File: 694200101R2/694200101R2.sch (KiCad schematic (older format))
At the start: 264 parts, among them J1 USB_C_Receptacle_USB2.0, J2 Conn_01x06_Male, SW1 MX_SW, SW10 MX_SW, SW100 MX_SW, SW101 MX_SW, SW102 MX_SW, SW103 MX_SW, SW104 MX_SW, SW105 MX_SW, SW106 MX_SW, SW107 MX_SW, SW108 SW_SPST, SW109 SW_SPDT, SW11 MX_SW, SW12 MX_SW, SW13 MX_SW, SW14 MX_SW, SW15 MX_SW, SW16 MX_SW, SW17 MX_SW, SW18 MX_SW, SW19 MX_SW, SW2 MX_SW, SW20 MX_SW, SW21 MX_SW, SW22 MX_SW, SW23 MX_SW, SW24 MX_SW, SW25 MX_SW, SW26 MX_SW, SW27 MX_SW, SW28 MX_SW, SW29 MX_SW, SW3 MX_SW, SW30 MX_SW, SW31 MX_SW, SW32 MX_SW, SW33 MX_SW, SW34 MX_SW, SW35 MX_SW, SW36 MX_SW, SW37 MX_SW, SW38 MX_SW, SW39 MX_SW, SW4 MX_SW, SW40 MX_SW, SW41 MX_SW, SW42 MX_SW, SW43 MX_SW, SW44 MX_SW, SW45 MX_SW, SW46 MX_SW, SW47 MX_SW, SW48 MX_SW, SW49 MX_SW, SW5 MX_SW, SW50 MX_SW, SW51 MX_SW, SW52 MX_SW, SW53 MX_SW, SW54 MX_SW, SW55 MX_SW, SW56 MX_SW, SW57 MX_SW, SW58 MX_SW, SW59 MX_SW, SW6 MX_SW, SW60 MX_SW, SW61 MX_SW, SW62 MX_SW, SW63 MX_SW, SW64 MX_SW, SW65 MX_SW, SW66 MX_SW, SW67 MX_SW, SW68 MX_SW, SW69 MX_SW, SW7 MX_SW, SW70 MX_SW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

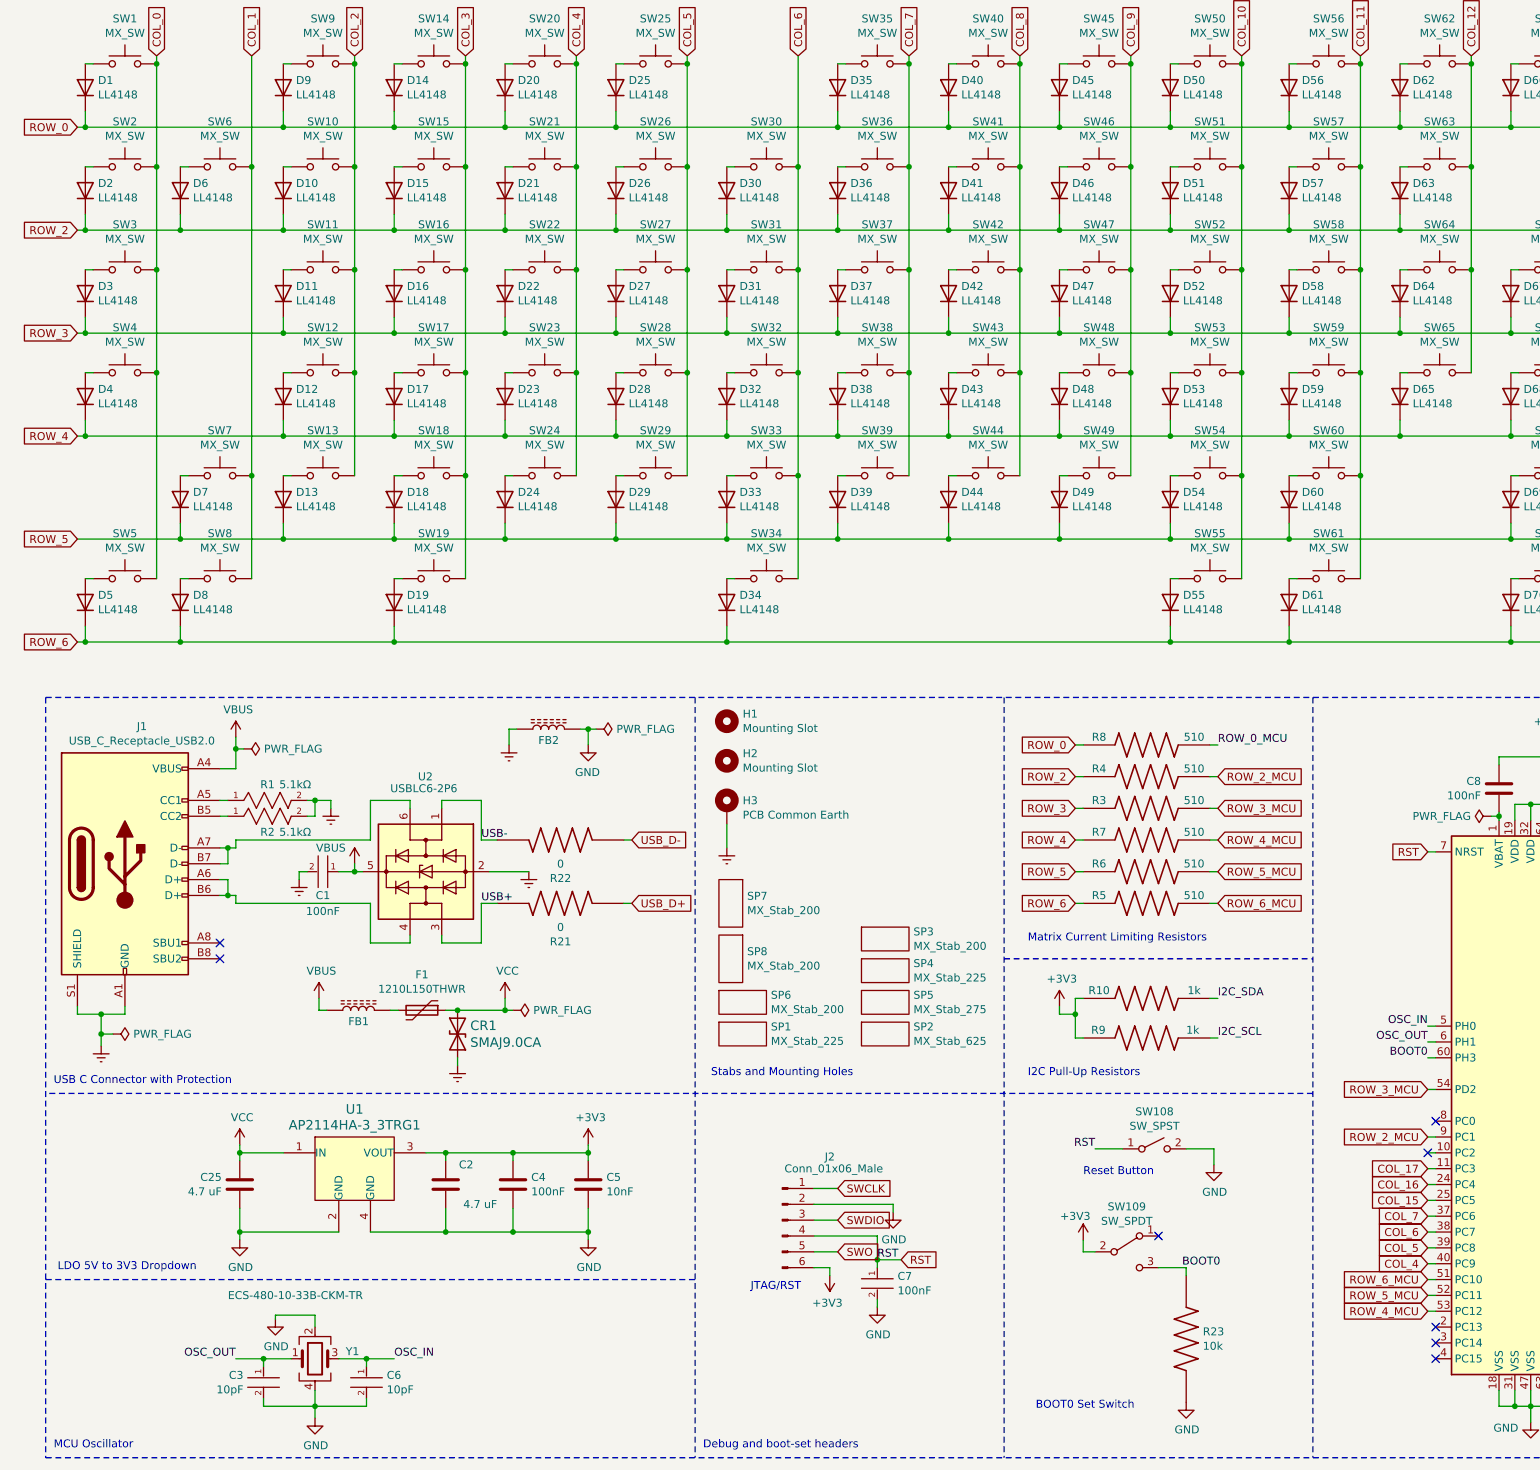
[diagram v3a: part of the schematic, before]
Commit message: Rename row labels
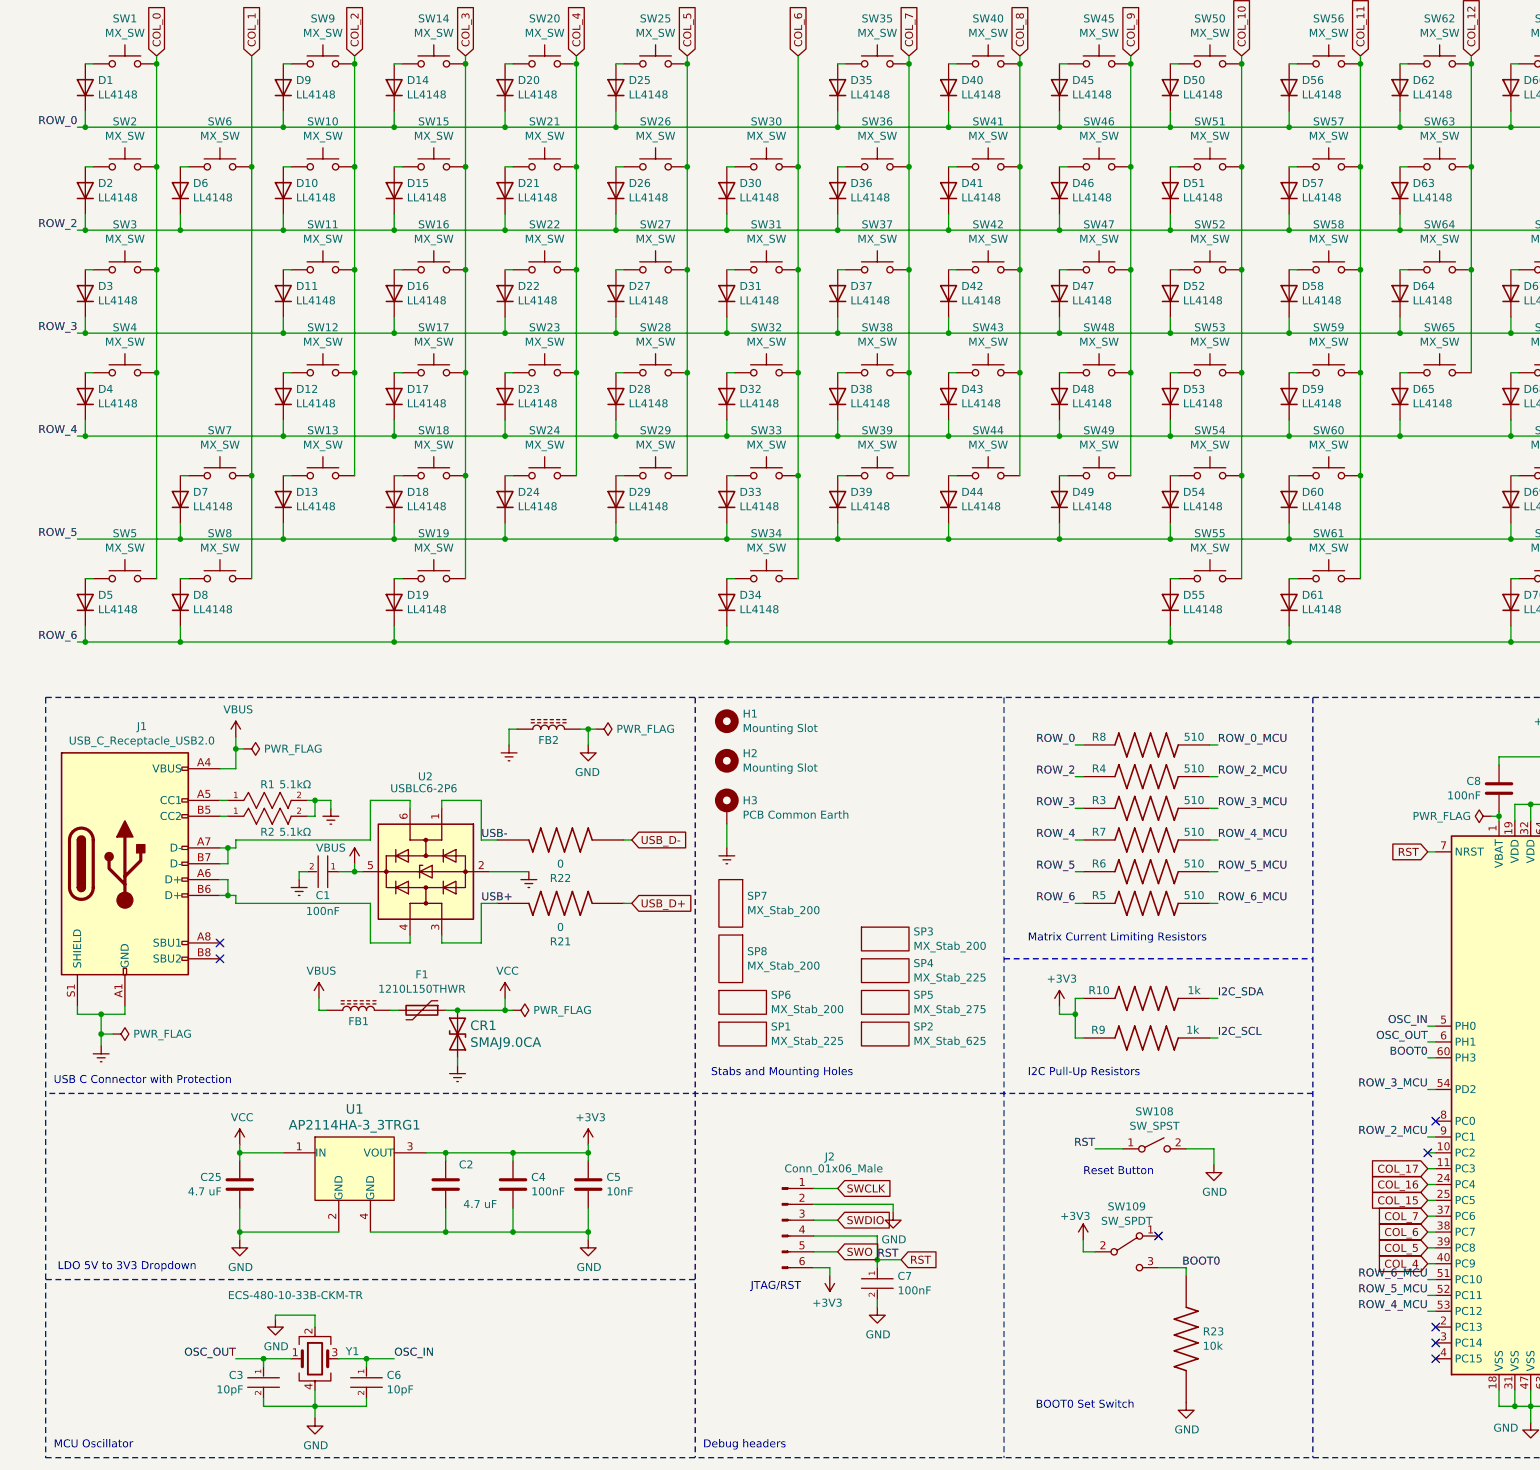
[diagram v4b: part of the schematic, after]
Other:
- note added: "Debug headers"
- note removed: "Debug and boot-set headers"
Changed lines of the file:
@@
 	1    0    0    -1
 $EndComp
-Text GLabel 850  1300 0    50   Input ~ 0
-ROW_0
 Text GLabel 1350 850  1    50   Input ~ 0
 COL_0
@@
 Wire Wire Line
 	900  3150 900  3250
-Text GLabel 850  1950 0    50   Input ~ 0
-ROW_2
-Text GLabel 850  2600 0    50   Input ~ 0
-ROW_3
-Text GLabel 850  3250 0    50   Input ~ 0
-ROW_4
-Text GLabel 850  3900 0    50   Input ~ 0
-ROW_5
-Text GLabel 850  4550 0    50   Input ~ 0
-ROW_6
 Text GLabel 1950 850  1    50   Input ~ 0
 COL_1
@@
 Text GLabel 10775 7375 2    50   Input ~ 0
 COL_0
-Text GLabel 7150 6200 0    50   Input ~ 0
-ROW_6
-Text GLabel 7150 6000 0    50   Input ~ 0
-ROW_5
-Text GLabel 7150 5800 0    50   Input ~ 0
-ROW_4
-Text GLabel 7150 5600 0    50   Input ~ 0
-ROW_3
-Text GLabel 7150 5200 0    50   Input ~ 0
-ROW_0
 $Comp
 L power:+3V3 #PWR014
@@
 Wire Wire Line
 	9825 5275 10125 5275
-Text GLabel 8050 5600 2    50   Input ~ 0
-ROW_3_MCU
 Wire Wire Line
 	8000 5600 8050 5600
-Text GLabel 9375 7375 0    50   Input ~ 0
-ROW_3_MCU
-Text GLabel 9375 7675 0    50   Input ~ 0
-ROW_2_MCU
-Text GLabel 9375 8575 0    50   Input ~ 0
-ROW_6_MCU
-Text GLabel 8050 6200 2    50   Input ~ 0
-ROW_6_MCU
 Wire Wire Line
 	8000 6200 8050 6200
-Text GLabel 8050 6000 2    50   Input ~ 0
-ROW_5_MCU
-Text GLabel 9375 8675 0    50   Input ~ 0
-ROW_5_MCU
-Text GLabel 8050 5800 2    50   Input ~ 0
-ROW_4_MCU
-Text GLabel 9375 8775 0    50   Input ~ 0
-ROW_4_MCU
 Wire Wire Line
 	8000 5400 8050 5400
-Text GLabel 8050 5400 2    50   Input ~ 0
-ROW_2_MCU
 $Comp
 L Resistor-Lib:RMCF0805FT510R R4
@@
 	1    0    0    -1
 $EndComp
-Text GLabel 7150 5400 0    50   Input ~ 0
-ROW_2
 Wire Wire Line
 	7200 5400 7150 5400
@@
 Encoder
 Text Notes 4800 9650 0    50   ~ 0
-Debug and boot-set headers
+Debug headers
 $Comp
 L power:PWR_FLAG #FLG0101
@@
 	9775 5650 9825 5650
 Connection ~ 9825 5650
-NoConn ~ 9375 7775
 NoConn ~ 10775 7975
 $Comp
@@
 Wire Wire Line
 	2025 9075 2200 9075
+Text Label 8050 5400 0    50   ~ 0
+ROW_2_MCU
+Text Label 8050 5600 0    50   ~ 0
+ROW_3_MCU
+Text Label 8050 5800 0    50   ~ 0
+ROW_4_MCU
+Text Label 8050 6000 0    50   ~ 0
+ROW_5_MCU
+Text Label 8050 6200 0    50   ~ 0
+ROW_6_MCU
+Text Label 9375 7675 2    50   ~ 0
+ROW_2_MCU
+Text Label 9375 7375 2    50   ~ 0
+ROW_3_MCU
+Text Label 9375 8775 2    50   ~ 0
+ROW_4_MCU
+Text Label 9375 8675 2    50   ~ 0
+ROW_5_MCU
+Text Label 9375 8575 2    50   ~ 0
+ROW_6_MCU
+Text Label 7150 5200 2    50   ~ 0
+ROW_0
+Text Label 7150 5400 2    50   ~ 0
+ROW_2
+Text Label 7150 5600 2    50   ~ 0
+ROW_3
+Text Label 7150 5800 2    50   ~ 0
+ROW_4
+Text Label 7150 6000 2    50   ~ 0
+ROW_5
+Text Label 7150 6200 2    50   ~ 0
+ROW_6
+Text Label 850  1300 2    50   ~ 0
+ROW_0
+Text Label 850  1950 2    50   ~ 0
+ROW_2
+Text Label 850  2600 2    50   ~ 0
+ROW_3
+Text Label 850  3250 2    50   ~ 0
+ROW_4
+Text Label 850  3900 2    50   ~ 0
+ROW_5
+Text Label 850  4550 2    50   ~ 0
+ROW_6
+NoConn ~ 9375 7775
 $EndSCHEMATC

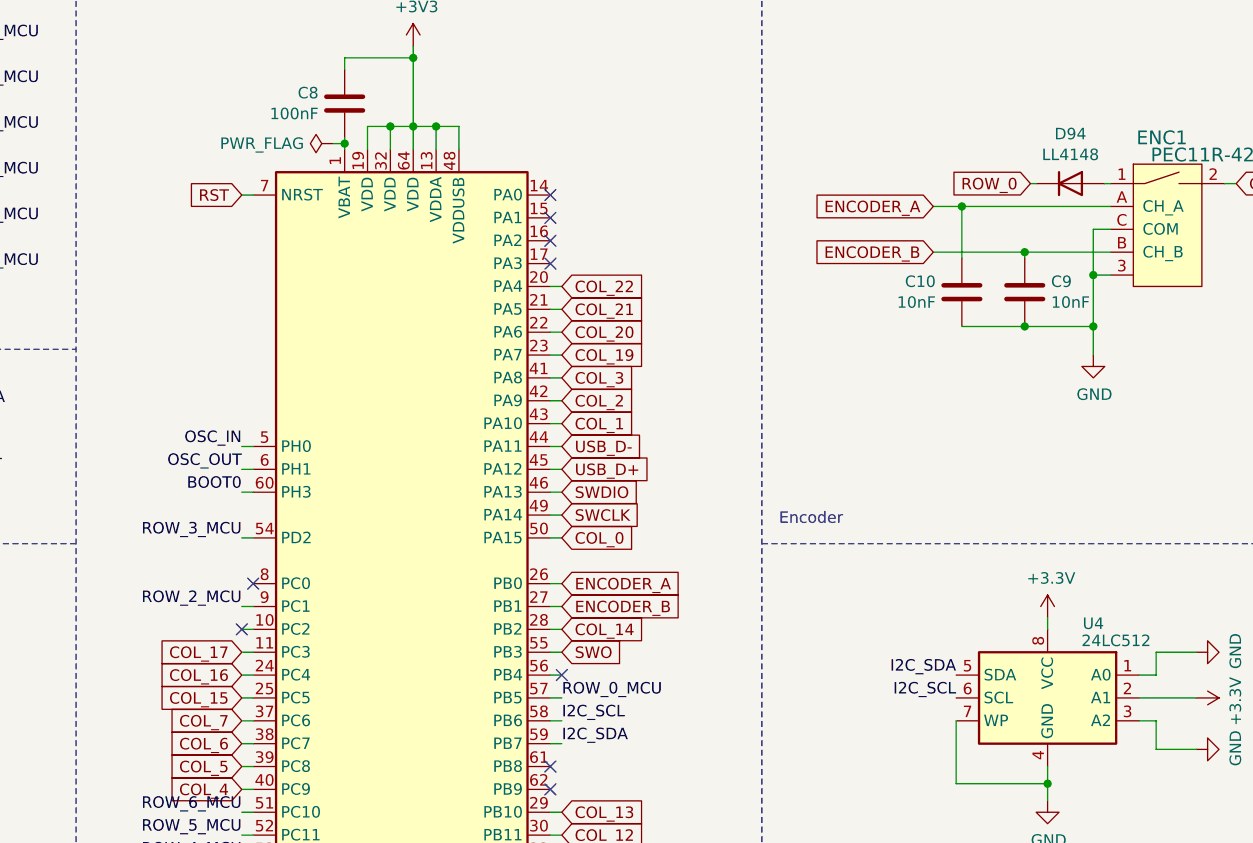
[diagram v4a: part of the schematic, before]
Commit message: Fixed Ratsnest errors from prettifying schematic
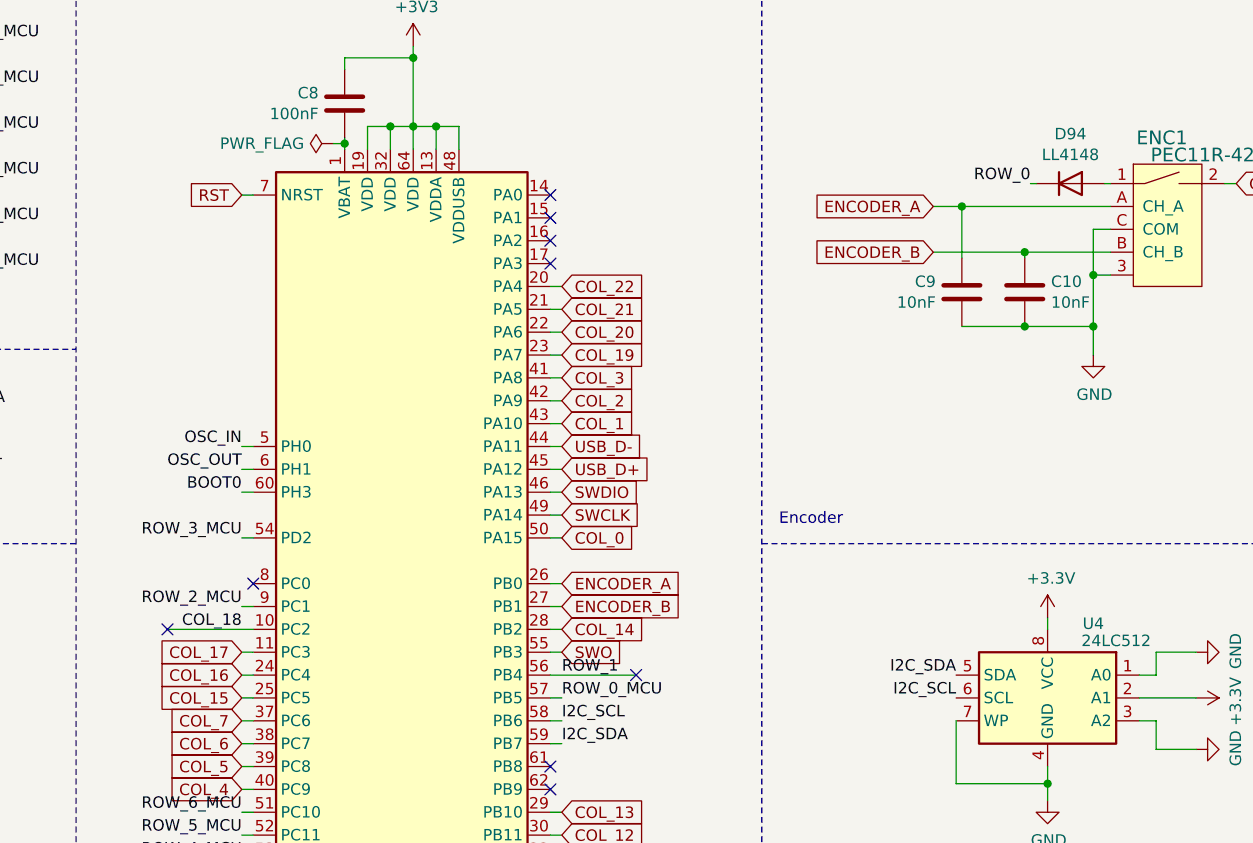
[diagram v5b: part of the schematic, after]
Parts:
- renumbered C9 to C10, C10 to C9
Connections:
- net COL_18: now reaches U3.10 (PC2)
- net ROW_1: now reaches U3.56 (PB4)
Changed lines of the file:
@@
 Wire Wire Line
 	12825 5825 12850 5825
-Text GLabel 12825 5825 0    50   Input ~ 0
-ROW_0
 Wire Wire Line
 	13175 6025 13100 6025
@@
 	12800 6125 12800 6150
 $Comp
-L Device:C C9
+L Device:C C10
 U 1 1 65C47B00
 P 12800 6300
-F 0 "C9" H 12915 6346 50  0000 L CNN
+F 0 "C10" H 12915 6346 50  0000 L CNN
 F 1 "10nF" H 12915 6255 50  0000 L CNN
 F 2 "Capacitor_SMD:C_0603_1608Metric" H 12838 6150 50  0001 C CNN
@@
 	13100 6025 13100 6225
 $Comp
-L Device:C C10
+L Device:C C9
 U 1 1 658CEFEB
 P 12525 6300
-F 0 "C10" H 12411 6346 50  0000 R CNN
+F 0 "C9" H 12411 6346 50  0000 R CNN
 F 1 "10nF" H 12411 6255 50  0000 R CNN
 F 2 "Capacitor_SMD:C_0603_1608Metric" H 12563 6150 50  0001 C CNN
@@
 	9775 5650 9825 5650
 Connection ~ 9825 5650
-NoConn ~ 10775 7975
+NoConn ~ 11100 7975
 $Comp
 L Power_Protection:USBLC6-2P6 U2
@@
 	9425 7875 9375 7875
 Wire Wire Line
-	9425 7775 9375 7775
+	9425 7775 9050 7775
 NoConn ~ 9425 9075
 NoConn ~ 9425 8975
@@
 	10725 8075 10775 8075
 Wire Wire Line
-	10725 7975 10775 7975
+	10725 7975 11100 7975
 Wire Wire Line
 	10725 7875 10775 7875
@@
 Text Label 850  4550 2    50   ~ 0
 ROW_6
-NoConn ~ 9375 7775
+NoConn ~ 9050 7775
+Text Label 12825 5825 2    50   ~ 0
+ROW_0
+Text Label 9375 7775 2    50   ~ 0
+COL_18
+Text Label 10775 7975 0    50   ~ 0
+ROW_1
 $EndSCHEMATC

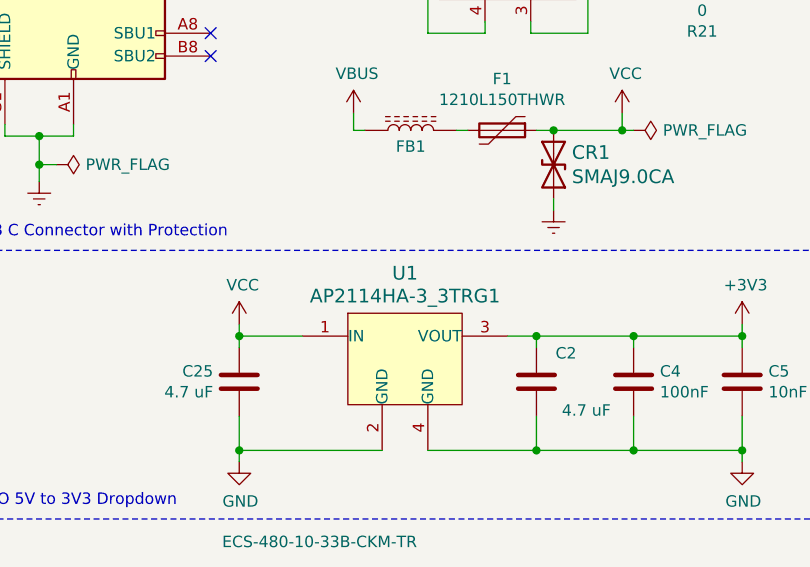
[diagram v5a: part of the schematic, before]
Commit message: Fixed Symbol for LDO
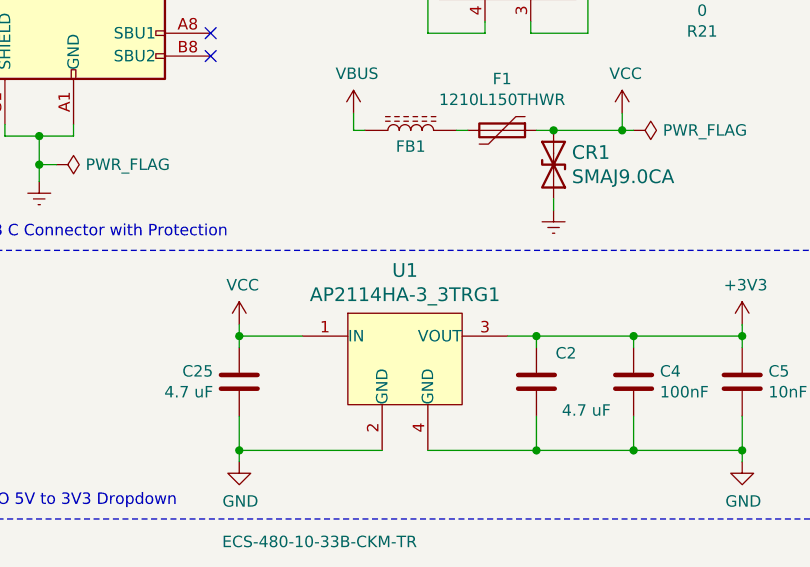
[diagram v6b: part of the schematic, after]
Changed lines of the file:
@@
-	1    0    0    -1
-$EndComp
-$Comp
-L cldg:AP2114HA-3_3TRG1 U1
-U 1 1 62A6A64D
-P 2650 7775
-F 0 "U1" H 2600 8050 60  0000 C CNN
-F 1 "AP2114HA-3_3TRG1" H 2600 7950 60  0000 C CNN
-F 2 "digikey-footprints:SOT-223" H 2850 7975 60  0001 L CNN
-F 3 "https://www.diodes.com/assets/Datasheets/AP2114.pdf" H 2850 8075 60  0001 L CNN
-F 4 "AP2114H-3.3TRG1DICT-ND" H 2850 8175 60  0001 L CNN "Digi-Key_PN"
-F 5 "AP2114H-3.3TRG1" H 2850 8275 60  0001 L CNN "MPN"
-F 6 "Integrated Circuits (ICs)" H 2850 8375 60  0001 L CNN "Category"
-F 7 "PMIC - Voltage Regulators - Linear" H 2850 8475 60  0001 L CNN "Family"
-F 8 "https://www.diodes.com/assets/Datasheets/AP2114.pdf" H 2850 8575 60  0001 L CNN "DK_Datasheet_Link"
-F 9 "/product-detail/en/diodes-incorporated/AP2114H-3.3TRG1/AP2114H-3.3TRG1DICT-ND/4505142" H 2850 8675 60  0001 L CNN "DK_Detail_Page"
-F 10 "IC REG LINEAR 3.3V 1A SOT223" H 2850 8775 60  0001 L CNN "Description"
-F 11 "Diodes Incorporated" H 2850 8875 60  0001 L CNN "Manufacturer"
-F 12 "Active" H 2850 8975 60  0001 L CNN "Status"
-	1    2650 7775
 	1    0    0    -1
 $EndComp
@@
 Text Label 10775 7975 0    50   ~ 0
 ROW_1
+$Comp
+L cldg:AP2114HA-3_3TRG1 U1
+U 1 1 632C3127
+P 2650 7775
+F 0 "U1" H 2600 8062 60  0000 C CNN
+F 1 "AP2114HA-3_3TRG1" H 2600 7956 60  0000 C CNN
+F 2 "digikey-footprints:SOT-223" H 2850 7975 60  0001 L CNN
+F 3 "https://www.diodes.com/assets/Datasheets/AP2114.pdf" H 2850 8075 60  0001 L CNN
+F 4 "AP2114H-3.3TRG1DICT-ND" H 2850 8175 60  0001 L CNN "Digi-Key_PN"
+F 5 "AP2114H-3.3TRG1" H 2850 8275 60  0001 L CNN "MPN"
+F 6 "Integrated Circuits (ICs)" H 2850 8375 60  0001 L CNN "Category"
+F 7 "PMIC - Voltage Regulators - Linear" H 2850 8475 60  0001 L CNN "Family"
+F 8 "https://www.diodes.com/assets/Datasheets/AP2114.pdf" H 2850 8575 60  0001 L CNN "DK_Datasheet_Link"
+F 9 "/product-detail/en/diodes-incorporated/AP2114H-3.3TRG1/AP2114H-3.3TRG1DICT-ND/4505142" H 2850 8675 60  0001 L CNN "DK_Detail_Page"
+F 10 "IC REG LINEAR 3.3V 1A SOT223" H 2850 8775 60  0001 L CNN "Description"
+F 11 "Diodes Incorporated" H 2850 8875 60  0001 L CNN "Manufacturer"
+F 12 "Active" H 2850 8975 60  0001 L CNN "Status"
+	1    2650 7775
+	1    0    0    -1
+$EndComp
 $EndSCHEMATC
